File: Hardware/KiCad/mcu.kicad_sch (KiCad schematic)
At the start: 24 parts, among them J1 USB_C, J2 Micro_SD_Card_Det, J3 STLink, U1 W25Q16, U2 USBLC6-2, U3 STM32F427ZGTx, Y1 8 MHz, Y2 32 kHz

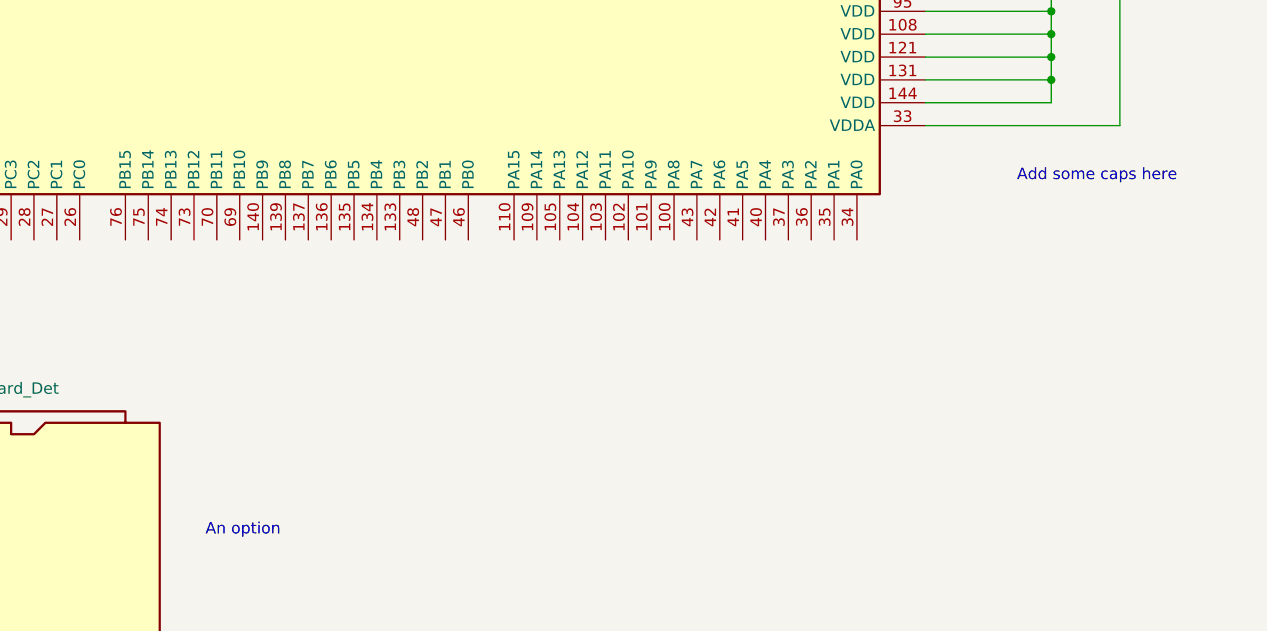
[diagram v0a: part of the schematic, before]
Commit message: Add decoupling capacitors and fix issue #7
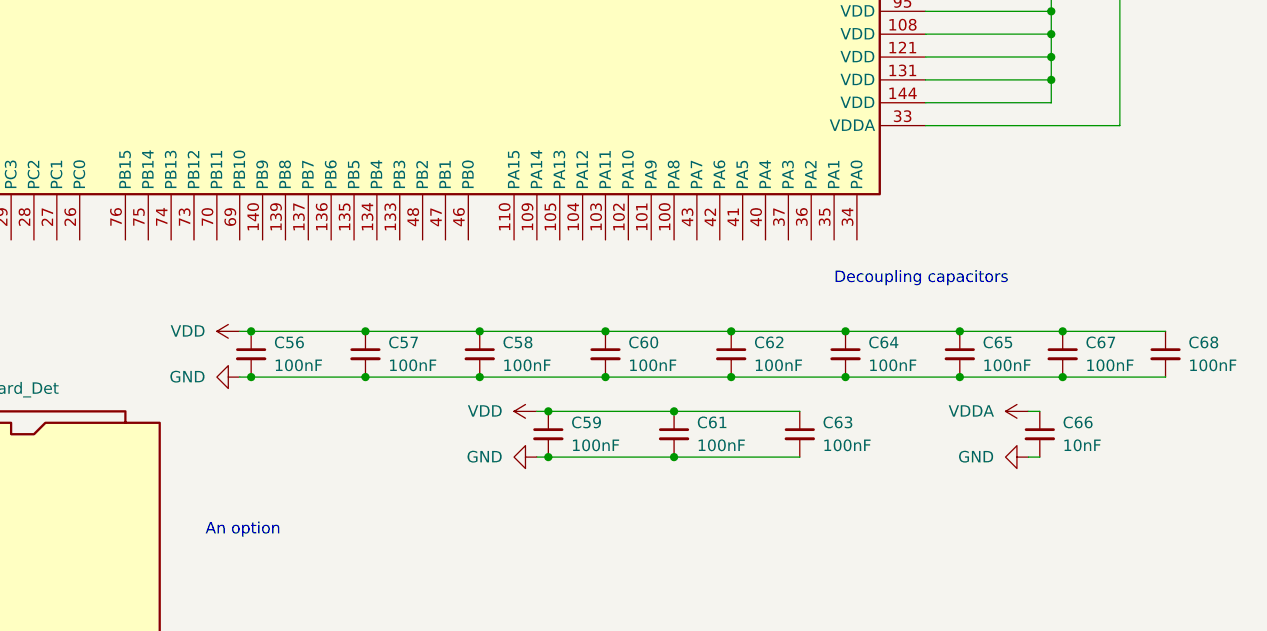
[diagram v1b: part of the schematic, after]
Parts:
- added C56, C57, C58, C59, C60, C61, C62, C63, C64, C65, C67, C68: 100nF, symbol Device:C_Small
- added C66: 10nF, symbol Device:C_Small
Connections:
- net GND: now also C56.2, C57.2, C58.2, C59.2, C60.2, C61.2, C62.2, C63.2, C64.2, C65.2, C66.2, C67.2, C68.2
- net VDD: now also C56.1, C57.1, C58.1, C59.1, C60.1, C61.1, C62.1, C63.1, C64.1, C65.1, C67.1, C68.1
- net VDDA: now also C66.1
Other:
- note added: "Decoupling capacitors"
- note removed: "Add some caps here"

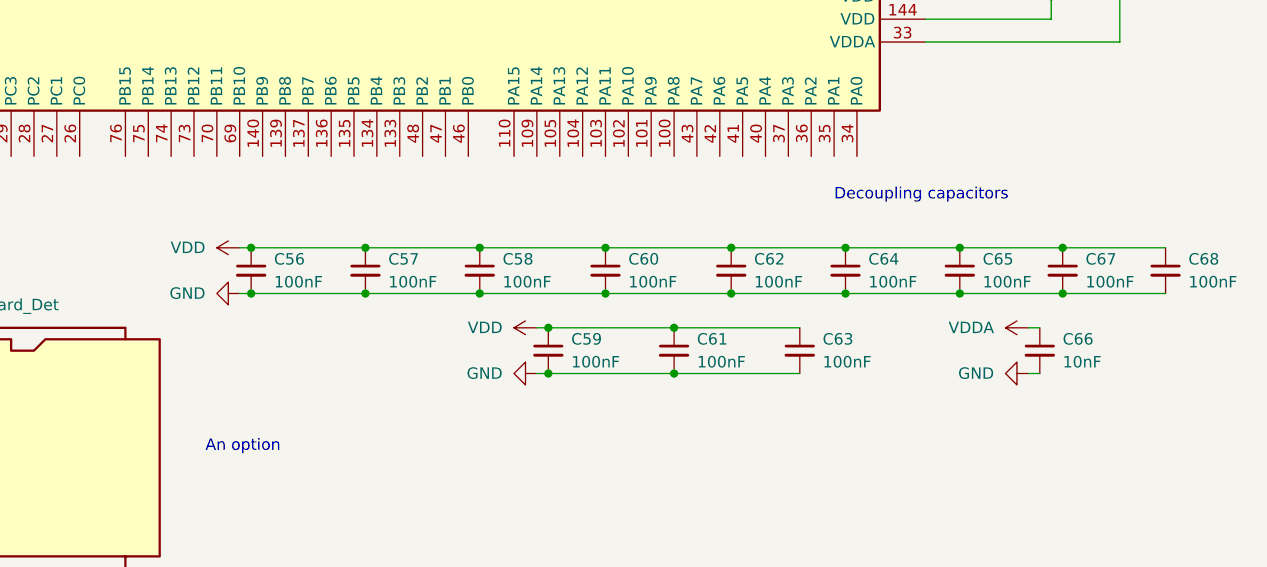
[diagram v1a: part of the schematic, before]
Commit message: Added footprints for decoupling caps
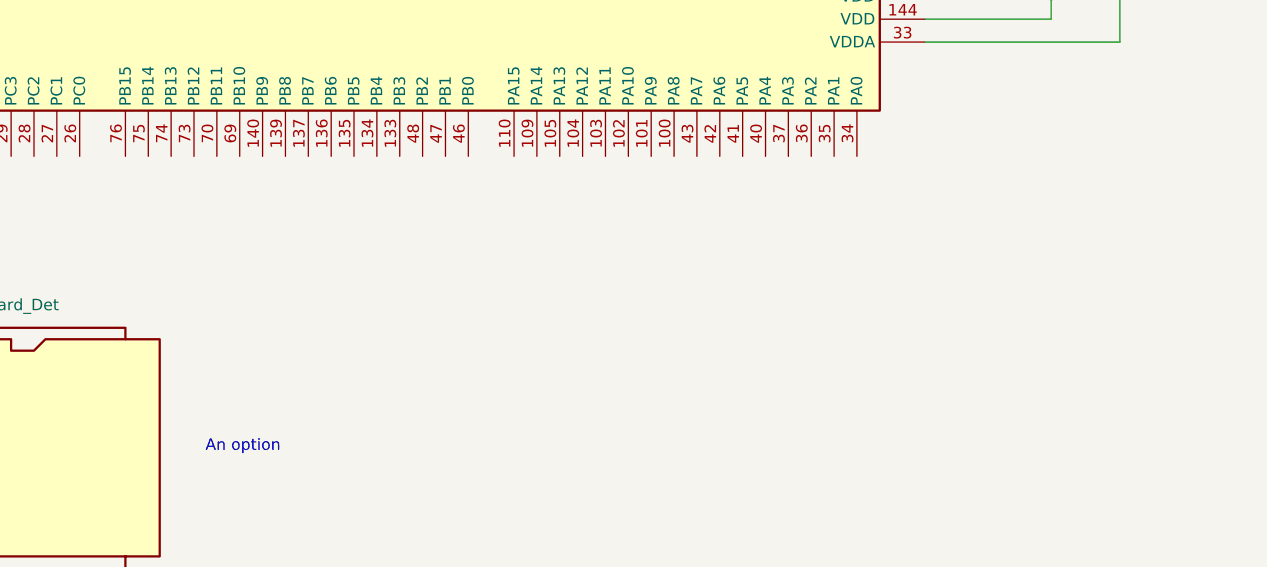
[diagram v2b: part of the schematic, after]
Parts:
- removed C56, C57, C58, C59, C60, C61, C62, C63, C64, C65, C67, C68: 100nF, symbol Device:C_Small
- removed C66: 10nF, symbol Device:C_Small
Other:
- note removed: "Decoupling capacitors"

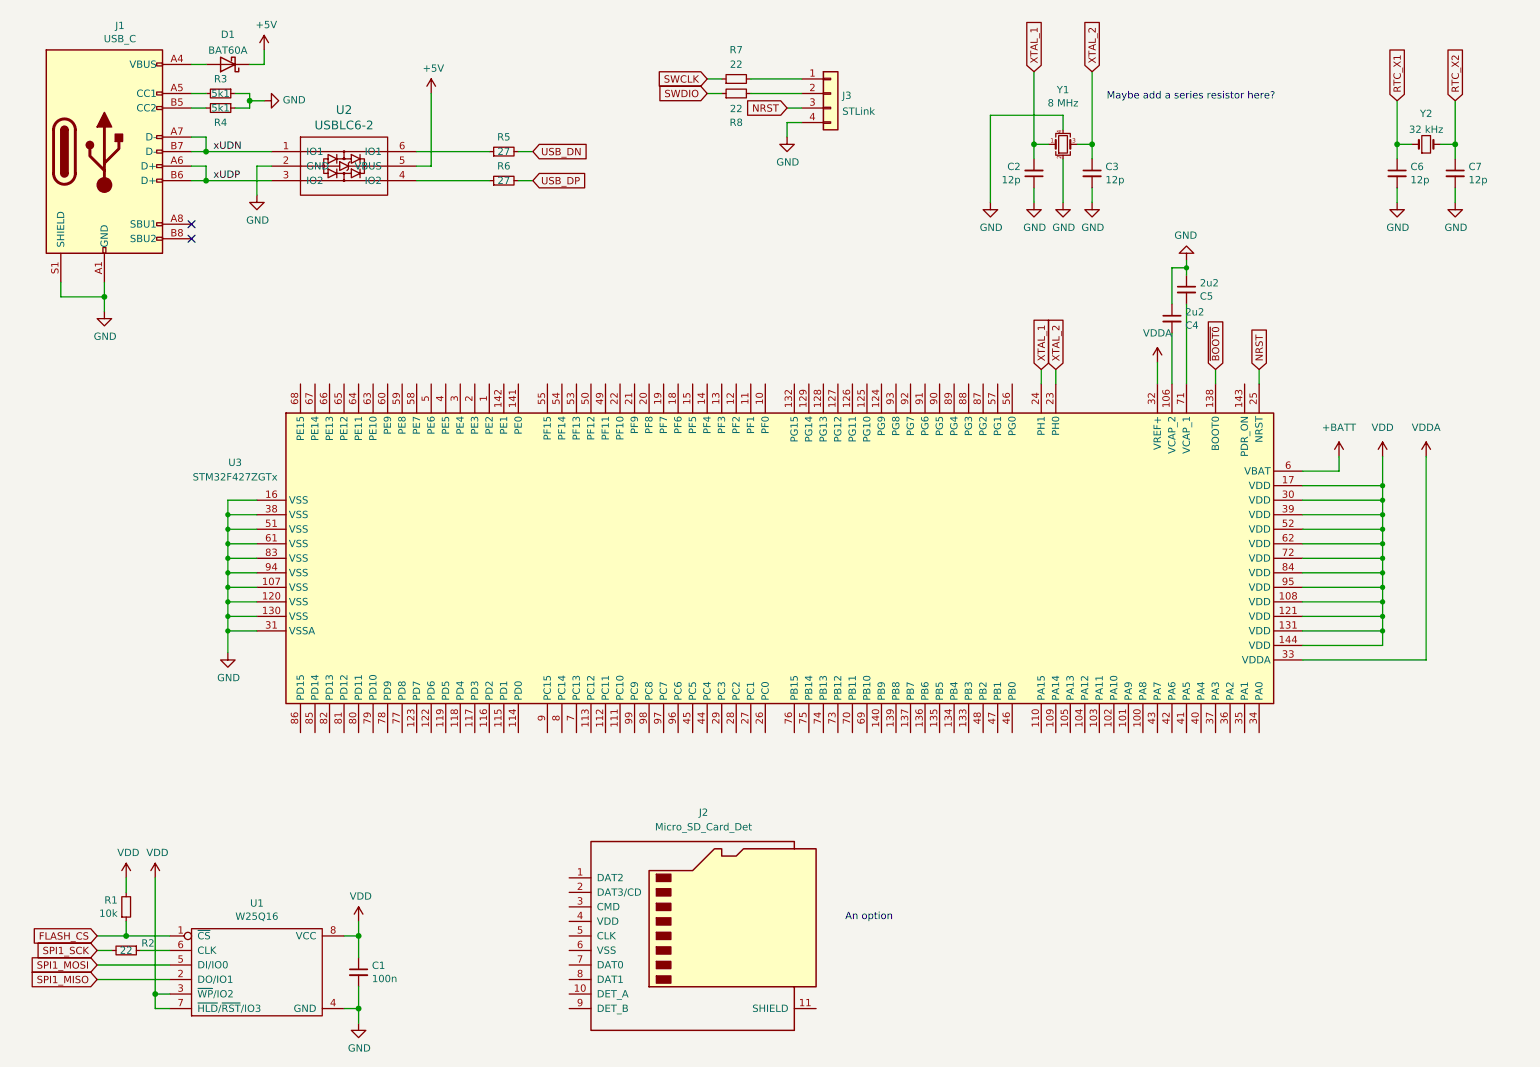
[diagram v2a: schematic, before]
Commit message: Connected SD card to the micro
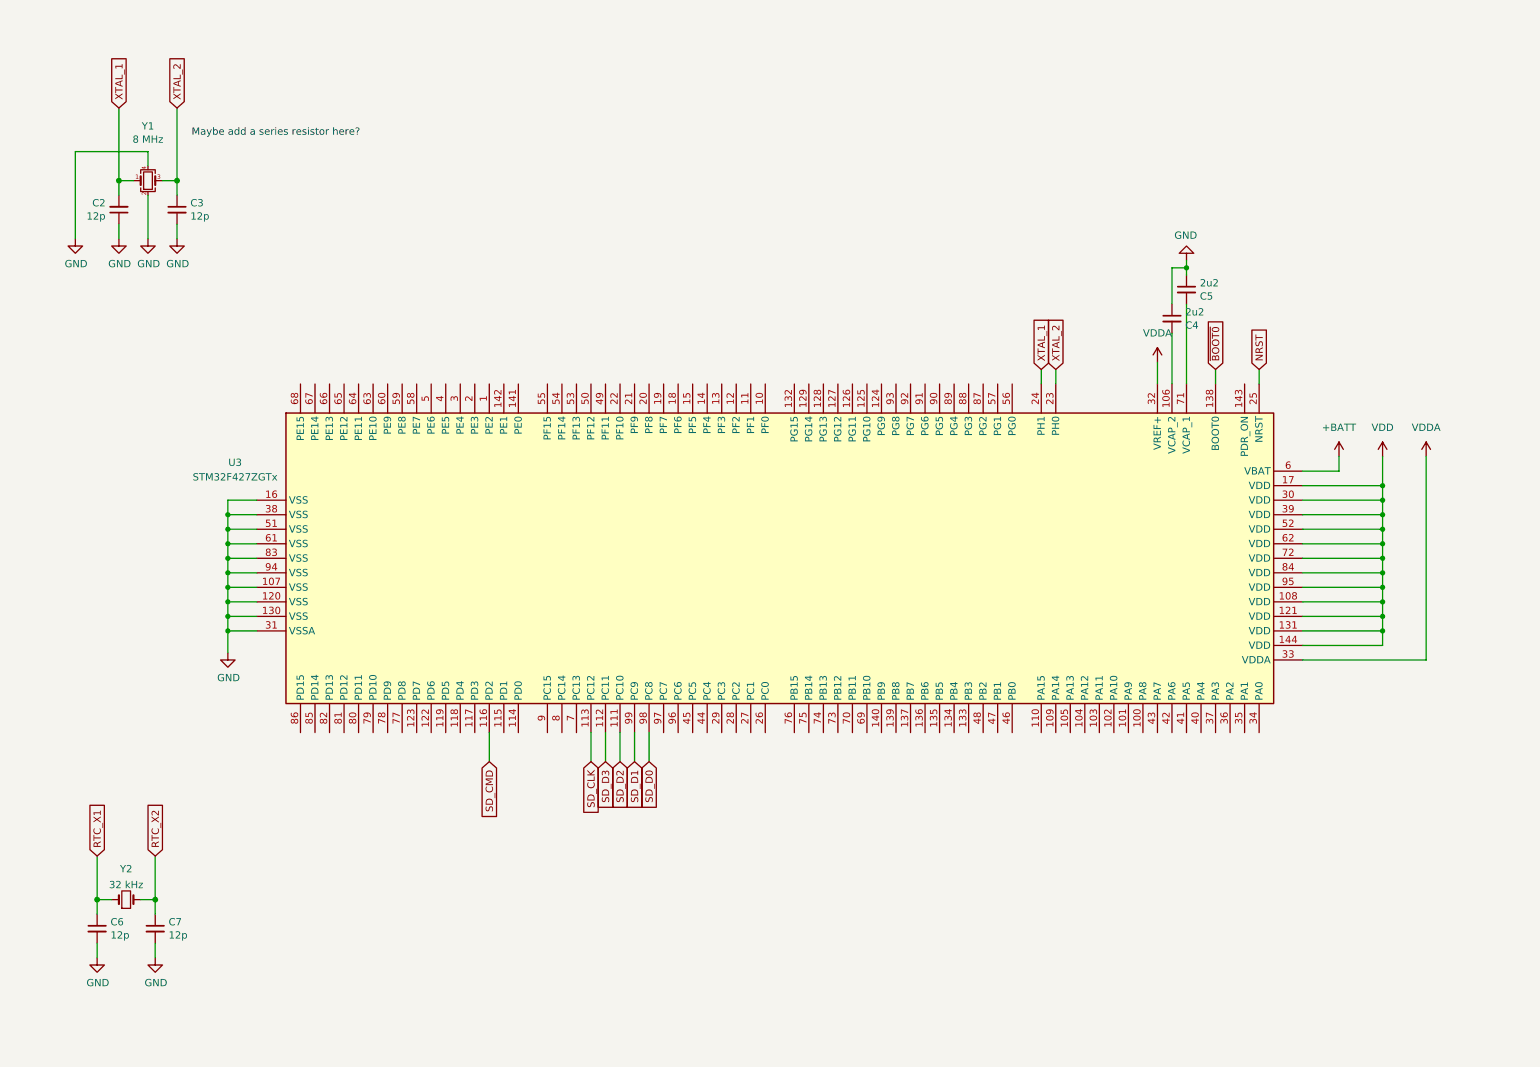
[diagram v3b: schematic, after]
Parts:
- removed C1: 100n, pkl_dipol:C_0603, symbol pkl_device:pkl_C_Small
- removed D1: BAT60A, Diode_SMD:D_SOD-323, symbol Diode:BAT60A
- removed J1: USB_C, pkl_connectors:USB_C_Receptacle_HRO_TYPE-C-31-M-12, symbol Connector:USB_C_Receptacle_USB2.0
- removed J2: Micro_SD_Card_Det, Connector_Card:microSD_HC_Hirose_DM3AT-SF-PEJM5, symbol Connector:Micro_SD_Card_Det
- removed J3: STLink, Connector_PinHeader_2.54mm:PinHeader_1x04_P2.54mm_Vertical, symbol Connector_Generic:Conn_01x04
- removed R1: 10k, pkl_dipol:R_0603, symbol pkl_device:pkl_R_Small
- removed R2: 22, pkl_dipol:R_0603, symbol pkl_device:pkl_R_Small
- removed R3, R4: 5k1, Resistor_SMD:R_0402_1005Metric, symbol pkl_device:pkl_R_Small
- removed R5, R6: 27, Resistor_SMD:R_0402_1005Metric, symbol pkl_device:pkl_R_Small
- removed R7, R8: 22, Resistor_SMD:R_0402_1005Metric, symbol pkl_device:pkl_R_Small
- removed U1: W25Q16, Package_SO:SOIC-8_3.9x4.9mm_P1.27mm, symbol pkl_memory:W25Q
- removed U2: USBLC6-2, pkl_housings_sot:SOT-23-6, symbol pkl_misc:USBLC6-2
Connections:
- net SD_D2: now reaches U3.111 (PC10)
- net SD_D3: now reaches U3.112 (PC11)
- net SD_CLK: now reaches U3.113 (PC12)
- net SD_CMD: now reaches U3.116 (PD2)
- net SD_D0: now reaches U3.98 (PC8)
- net SD_D1: now reaches U3.99 (PC9)
- no-connect marks 2 -> 0
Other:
- note removed: "An option"
- moved on the sheet: C2, C3, C6, C7, Y1, Y2

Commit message: Added some connections
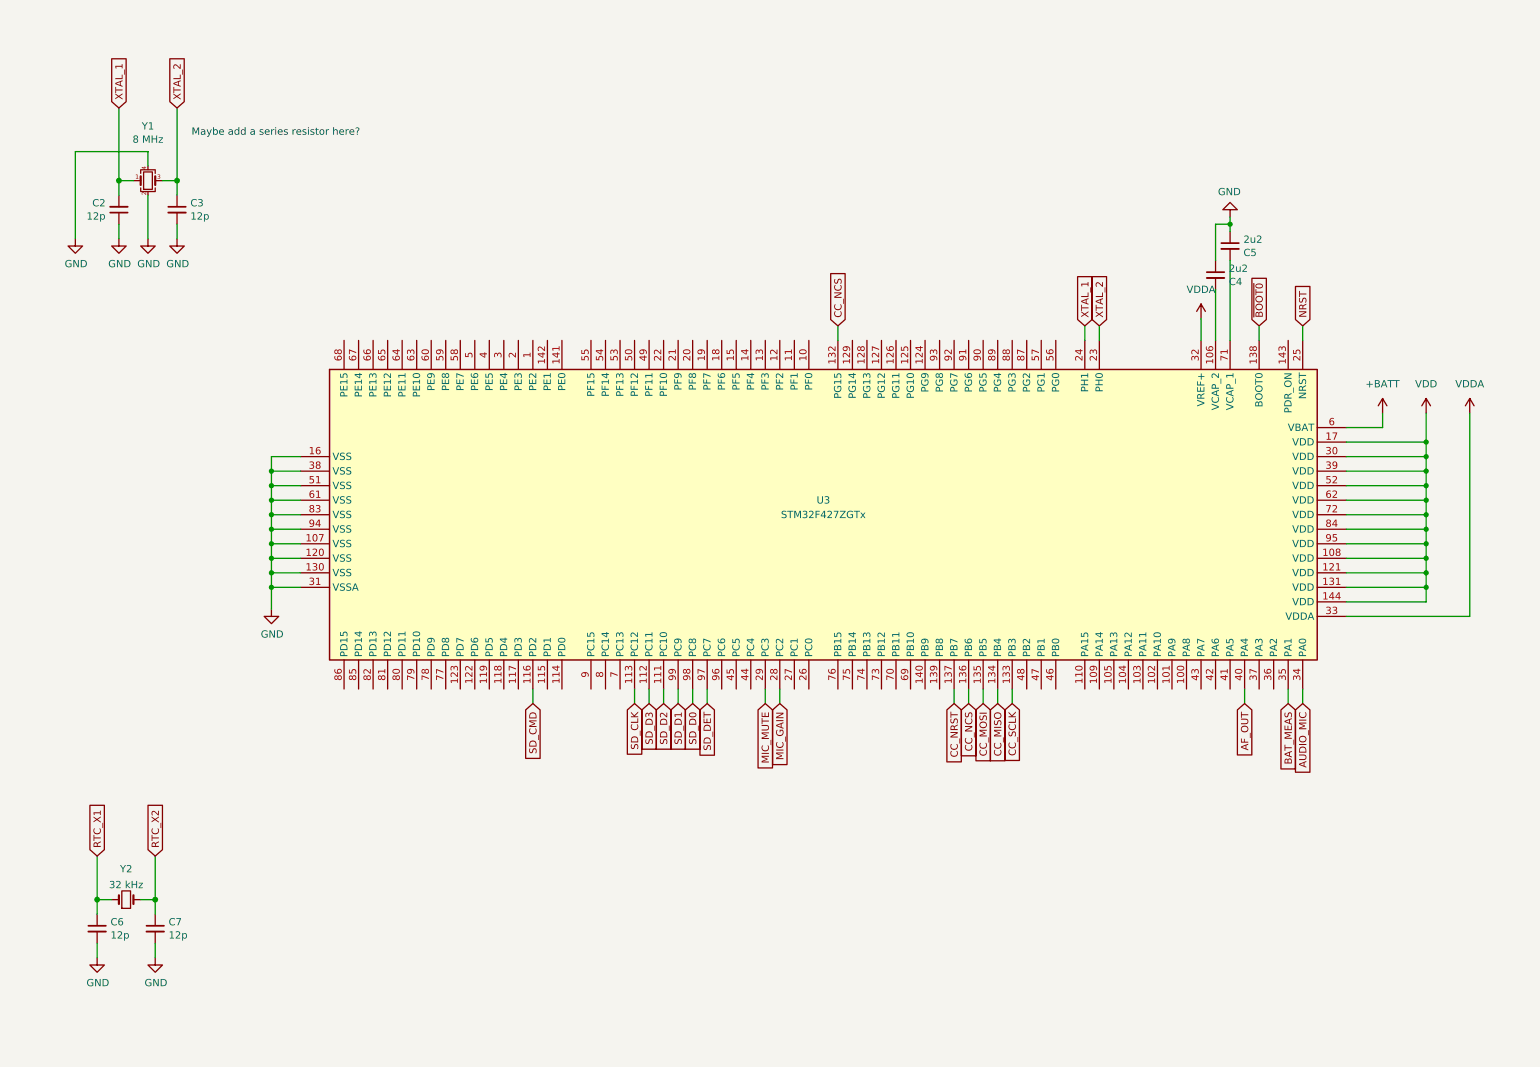
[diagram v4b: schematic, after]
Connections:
- net CC_NCS: now reaches U3.132 (PG15)
- net CC_NCS: now also U3.136 (PB6)
- net CC_SCLK: now reaches U3.133 (PB3)
- net CC_MISO: now reaches U3.134 (PB4)
- net CC_MOSI: now reaches U3.135 (PB5)
- net CC_NRST: now reaches U3.137 (PB7)
- net MIC_GAIN: now reaches U3.28 (PC2)
- net MIC_MUTE: now reaches U3.29 (PC3)
- net AUDIO_MIC: now reaches U3.34 (PA0)
- net BAT_MEAS: now reaches U3.35 (PA1)
- net AF_OUT: now reaches U3.40 (PA4)
- net SD_DET: now reaches U3.97 (PC7)
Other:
- moved on the sheet: C4, C5, U3
